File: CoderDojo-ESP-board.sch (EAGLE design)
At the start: 85 parts, among them IC1 ESP-12E/F, IC2 FT232RL, IC3 L293D, U1 PCA9685PW,118, U2 AMS1117-3.3, U3 MCP23017-E/SO, X1 PN61729-S

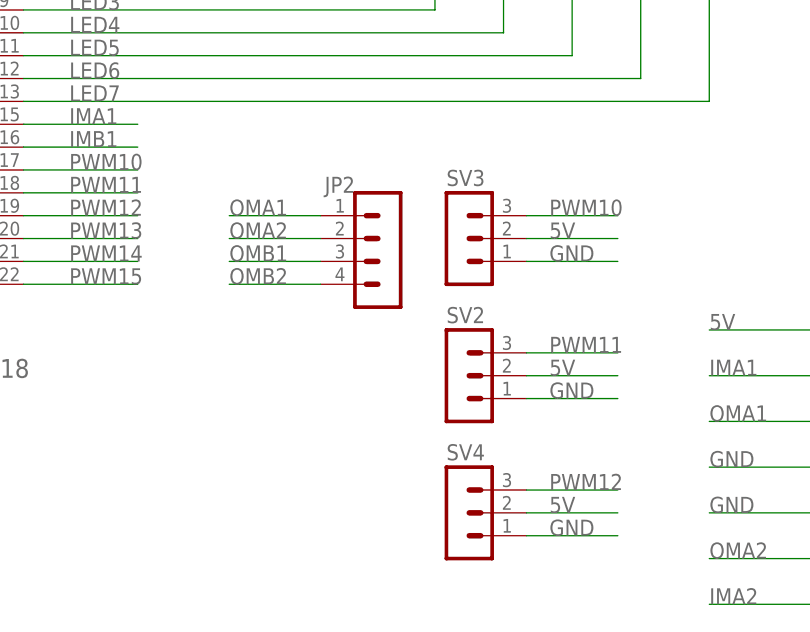
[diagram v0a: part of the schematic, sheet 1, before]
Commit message: add board eagle file
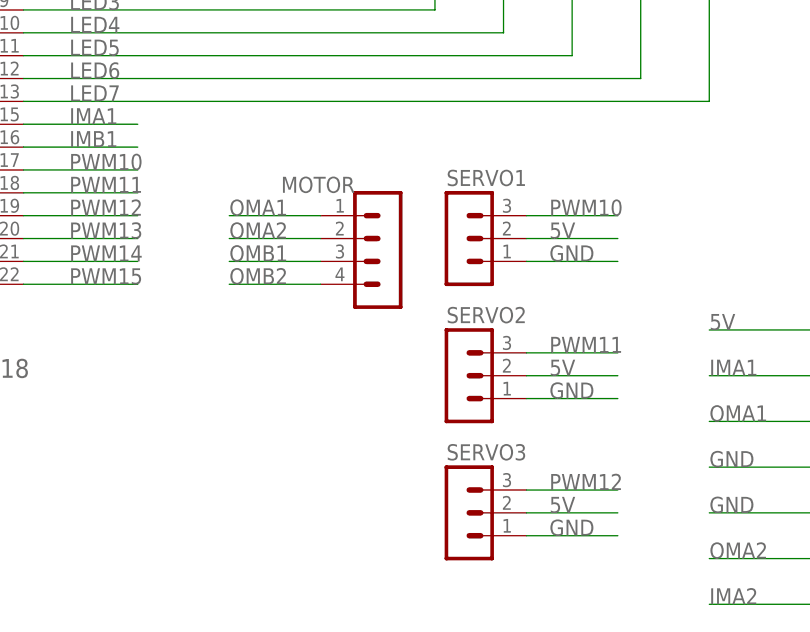
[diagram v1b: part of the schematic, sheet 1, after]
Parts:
- renumbered JP2 to MOTOR, SV2 to SERVO2, SV3 to SERVO1, SV4 to SERVO3
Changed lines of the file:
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@@
 <part name="R24" library="rcl" library_urn="urn:adsk.eagle:library:334" deviceset="R-EU_" device="R0805" package3d_urn="urn:adsk.eagle:package:23553/2" value="10K"/>
 <part name="C8" library="rcl" library_urn="urn:adsk.eagle:library:334" deviceset="C-EU" device="C0805" package3d_urn="urn:adsk.eagle:package:23617/2" value="0.1µF"/>
-<part name="JP2" library="con-lstb" library_urn="urn:adsk.eagle:library:162" deviceset="MA04-1" device="" package3d_urn="urn:adsk.eagle:package:8337/1"/>
+<part name="MOTOR" library="con-lstb" library_urn="urn:adsk.eagle:library:162" deviceset="MA04-1" device="" package3d_urn="urn:adsk.eagle:package:8337/1"/>
 <part name="R25" library="rcl" library_urn="urn:adsk.eagle:library:334" deviceset="R-EU_" device="R0805" package3d_urn="urn:adsk.eagle:package:23553/2" value="10K"/>
 <part name="R26" library="rcl" library_urn="urn:adsk.eagle:library:334" deviceset="R-EU_" device="R0805" package3d_urn="urn:adsk.eagle:package:23553/2" value="10K"/>
@@
 <part name="C9" library="rcl" library_urn="urn:adsk.eagle:library:334" deviceset="CPOL-EU" device="E2-5" package3d_urn="urn:adsk.eagle:package:23346/2" value="10µF"/>
 <part name="SV1" library="con-lsta" library_urn="urn:adsk.eagle:library:161" deviceset="FE20-2" device="" package3d_urn="urn:adsk.eagle:package:8184/1"/>
-<part name="SV2" library="con-lstb" library_urn="urn:adsk.eagle:library:162" deviceset="MA03-1" device="" package3d_urn="urn:adsk.eagle:package:8339/1"/>
-<part name="SV3" library="con-lstb" library_urn="urn:adsk.eagle:library:162" deviceset="MA03-1" device="" package3d_urn="urn:adsk.eagle:package:8339/1"/>
-<part name="SV4" library="con-lstb" library_urn="urn:adsk.eagle:library:162" deviceset="MA03-1" device="" package3d_urn="urn:adsk.eagle:package:8339/1"/>
+<part name="SERVO2" library="con-lstb" library_urn="urn:adsk.eagle:library:162" deviceset="MA03-1" device="" package3d_urn="urn:adsk.eagle:package:8339/1"/>
+<part name="SERVO1" library="con-lstb" library_urn="urn:adsk.eagle:library:162" deviceset="MA03-1" device="" package3d_urn="urn:adsk.eagle:package:8339/1"/>
+<part name="SERVO3" library="con-lstb" library_urn="urn:adsk.eagle:library:162" deviceset="MA03-1" device="" package3d_urn="urn:adsk.eagle:package:8339/1"/>
 <part name="C4" library="rcl" library_urn="urn:adsk.eagle:library:334" deviceset="CPOL-EU" device="E2-5" package3d_urn="urn:adsk.eagle:package:23346/2" value="10µF"/>
 <part name="GND11" library="supply1" library_urn="urn:adsk.eagle:library:371" deviceset="GND" device=""/>
@@
 <attribute name="VALUE" x="4.064" y="20.701" size="1.778" layer="96"/>
 </instance>
-<instance part="JP2" gate="1" x="251.46" y="114.3" smashed="yes" rot="R180">
+<instance part="MOTOR" gate="1" x="251.46" y="114.3" smashed="yes" rot="R180">
 <attribute name="VALUE" x="252.73" y="124.46" size="1.778" layer="96" rot="R180"/>
 <attribute name="NAME" x="247.65" y="123.698" size="1.778" layer="95" rot="R180"/>
@@
 <attribute name="NAME" x="186.69" y="231.902" size="1.778" layer="95"/>
 </instance>
-<instance part="SV2" gate="G$1" x="259.08" y="101.6" smashed="yes">
+<instance part="SERVO2" gate="G$1" x="259.08" y="101.6" smashed="yes">
 <attribute name="VALUE" x="257.81" y="93.98" size="1.778" layer="96"/>
 <attribute name="NAME" x="257.81" y="107.442" size="1.778" layer="95"/>
 </instance>
-<instance part="SV3" gate="G$1" x="259.08" y="116.84" smashed="yes">
+<instance part="SERVO1" gate="G$1" x="259.08" y="116.84" smashed="yes">
 <attribute name="VALUE" x="257.81" y="109.22" size="1.778" layer="96"/>
 <attribute name="NAME" x="257.81" y="122.682" size="1.778" layer="95"/>
 </instance>
-<instance part="SV4" gate="G$1" x="259.08" y="86.36" smashed="yes">
+<instance part="SERVO3" gate="G$1" x="259.08" y="86.36" smashed="yes">
 <attribute name="VALUE" x="257.81" y="78.74" size="1.778" layer="96"/>
 <attribute name="NAME" x="257.81" y="92.202" size="1.778" layer="95"/>
@@
 </segment>
 <segment>
-<pinref part="SV3" gate="G$1" pin="1"/>
+<pinref part="SERVO1" gate="G$1" pin="1"/>
 <wire x1="266.7" y1="114.3" x2="276.86" y2="114.3" width="0.1524" layer="91"/>
 <label x="269.24" y="114.3" size="1.778" layer="95"/>
 </segment>
 <segment>
-<pinref part="SV2" gate="G$1" pin="1"/>
+<pinref part="SERVO2" gate="G$1" pin="1"/>
 <wire x1="266.7" y1="99.06" x2="276.86" y2="99.06" width="0.1524" layer="91"/>
 <label x="269.24" y="99.06" size="1.778" layer="95"/>
 </segment>
 <segment>
-<pinref part="SV4" gate="G$1" pin="1"/>
+<pinref part="SERVO3" gate="G$1" pin="1"/>
 <wire x1="266.7" y1="83.82" x2="276.86" y2="83.82" width="0.1524" layer="91"/>
 <label x="269.24" y="83.82" size="1.778" layer="95"/>
@@
 </segment>
 <segment>
-<pinref part="SV3" gate="G$1" pin="3"/>
+<pinref part="SERVO1" gate="G$1" pin="3"/>
 <wire x1="266.7" y1="119.38" x2="276.86" y2="119.38" width="0.1524" layer="91"/>
 <label x="269.24" y="119.38" size="1.778" layer="95"/>
@@
 </segment>
 <segment>
-<pinref part="SV2" gate="G$1" pin="3"/>
+<pinref part="SERVO2" gate="G$1" pin="3"/>
 <wire x1="266.7" y1="104.14" x2="276.86" y2="104.14" width="0.1524" layer="91"/>
 <label x="269.24" y="104.14" size="1.778" layer="95"/>
@@
 </segment>
 <segment>
-<pinref part="SV4" gate="G$1" pin="3"/>
+<pinref part="SERVO3" gate="G$1" pin="3"/>
 <wire x1="266.7" y1="88.9" x2="276.86" y2="88.9" width="0.1524" layer="91"/>
 <label x="269.24" y="88.9" size="1.778" layer="95"/>
@@
 </segment>
 <segment>
-<pinref part="SV3" gate="G$1" pin="2"/>
+<pinref part="SERVO1" gate="G$1" pin="2"/>
 <wire x1="266.7" y1="116.84" x2="276.86" y2="116.84" width="0.1524" layer="91"/>
 <label x="269.24" y="116.84" size="1.778" layer="95"/>
 </segment>
 <segment>
-<pinref part="SV2" gate="G$1" pin="2"/>
+<pinref part="SERVO2" gate="G$1" pin="2"/>
 <wire x1="266.7" y1="101.6" x2="276.86" y2="101.6" width="0.1524" layer="91"/>
 <label x="269.24" y="101.6" size="1.778" layer="95"/>
 </segment>
 <segment>
-<pinref part="SV4" gate="G$1" pin="2"/>
+<pinref part="SERVO3" gate="G$1" pin="2"/>
 <wire x1="266.7" y1="86.36" x2="276.86" y2="86.36" width="0.1524" layer="91"/>
 <label x="269.24" y="86.36" size="1.778" layer="95"/>
@@
 </segment>
 <segment>
-<pinref part="JP2" gate="1" pin="1"/>
+<pinref part="MOTOR" gate="1" pin="1"/>
 <wire x1="243.84" y1="119.38" x2="233.68" y2="119.38" width="0.1524" layer="91"/>
 <label x="233.68" y="119.38" size="1.778" layer="95"/>
@@
 </segment>
 <segment>
-<pinref part="JP2" gate="1" pin="2"/>
+<pinref part="MOTOR" gate="1" pin="2"/>
 <wire x1="243.84" y1="116.84" x2="233.68" y2="116.84" width="0.1524" layer="91"/>
 <label x="233.68" y="116.84" size="1.778" layer="95"/>
@@
 </segment>
 <segment>
-<pinref part="JP2" gate="1" pin="3"/>
+<pinref part="MOTOR" gate="1" pin="3"/>
 <wire x1="243.84" y1="114.3" x2="233.68" y2="114.3" width="0.1524" layer="91"/>
 <label x="233.68" y="114.3" size="1.778" layer="95"/>
@@
 </segment>
 <segment>
-<pinref part="JP2" gate="1" pin="4"/>
+<pinref part="MOTOR" gate="1" pin="4"/>
 <wire x1="243.84" y1="111.76" x2="233.68" y2="111.76" width="0.1524" layer="91"/>
 <label x="233.68" y="111.76" size="1.778" layer="95"/>
